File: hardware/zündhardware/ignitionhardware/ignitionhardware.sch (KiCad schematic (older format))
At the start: 25 parts

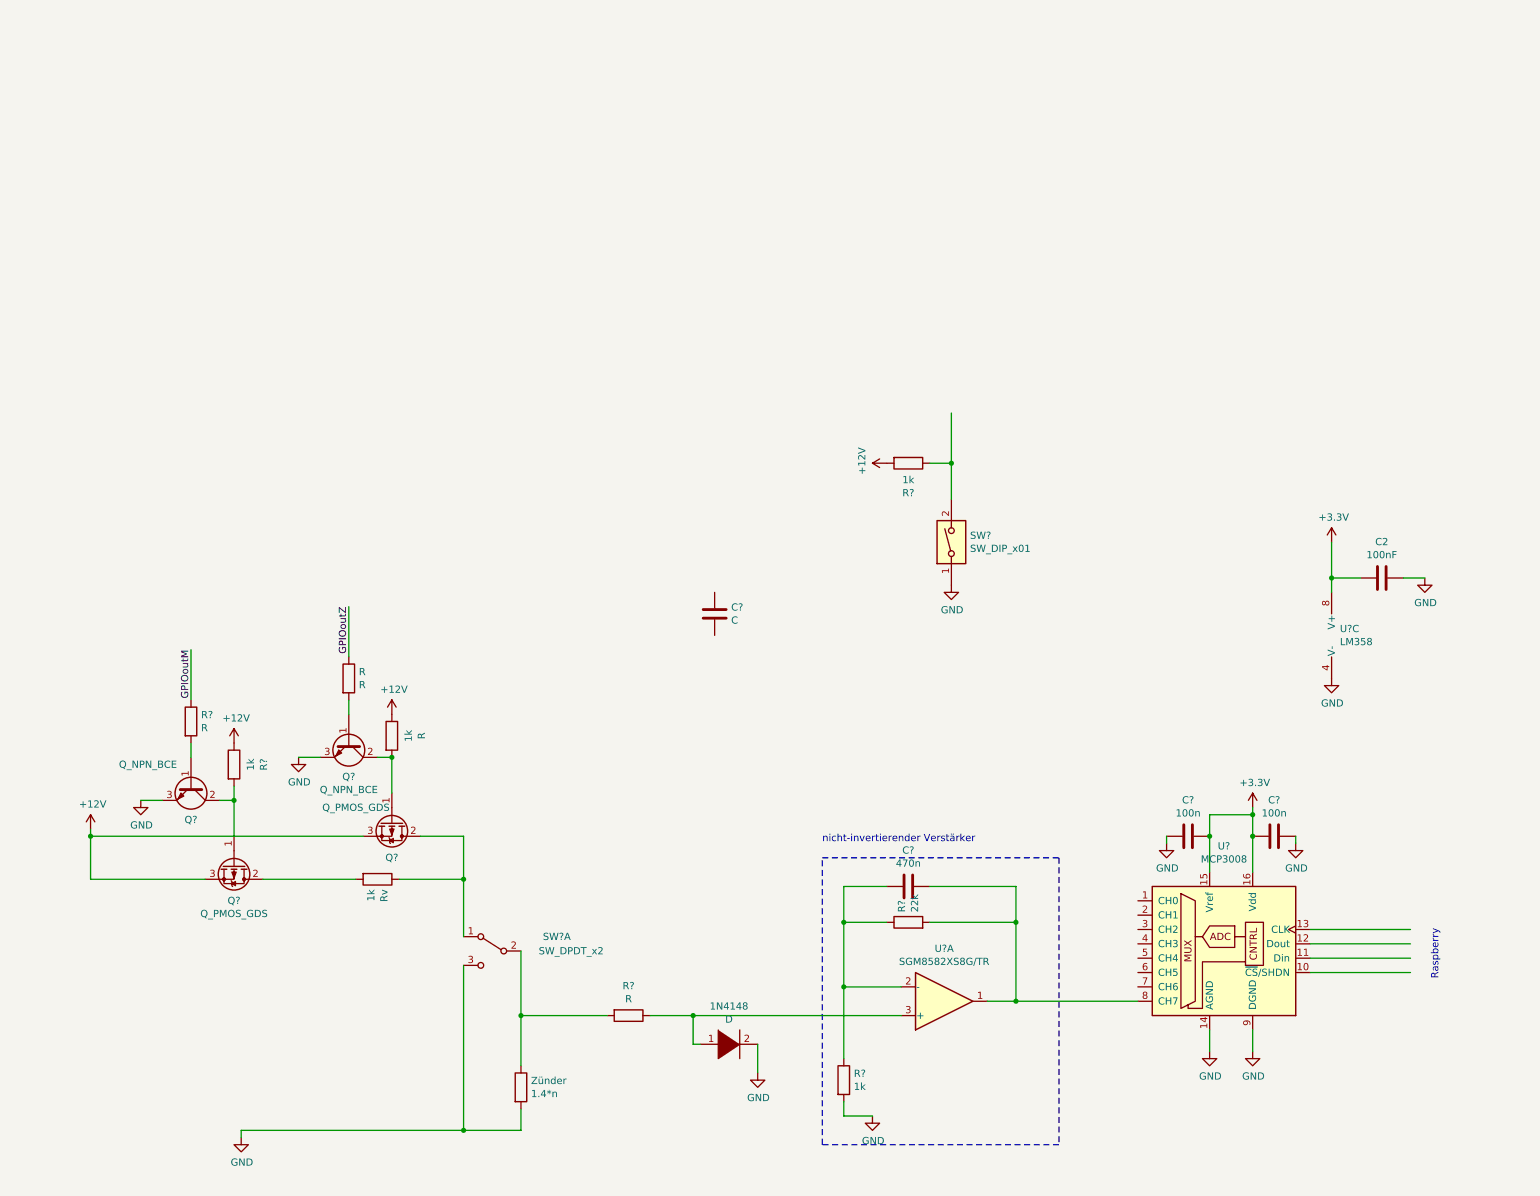
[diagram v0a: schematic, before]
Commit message: updated ignition hardware and created asciidoc description
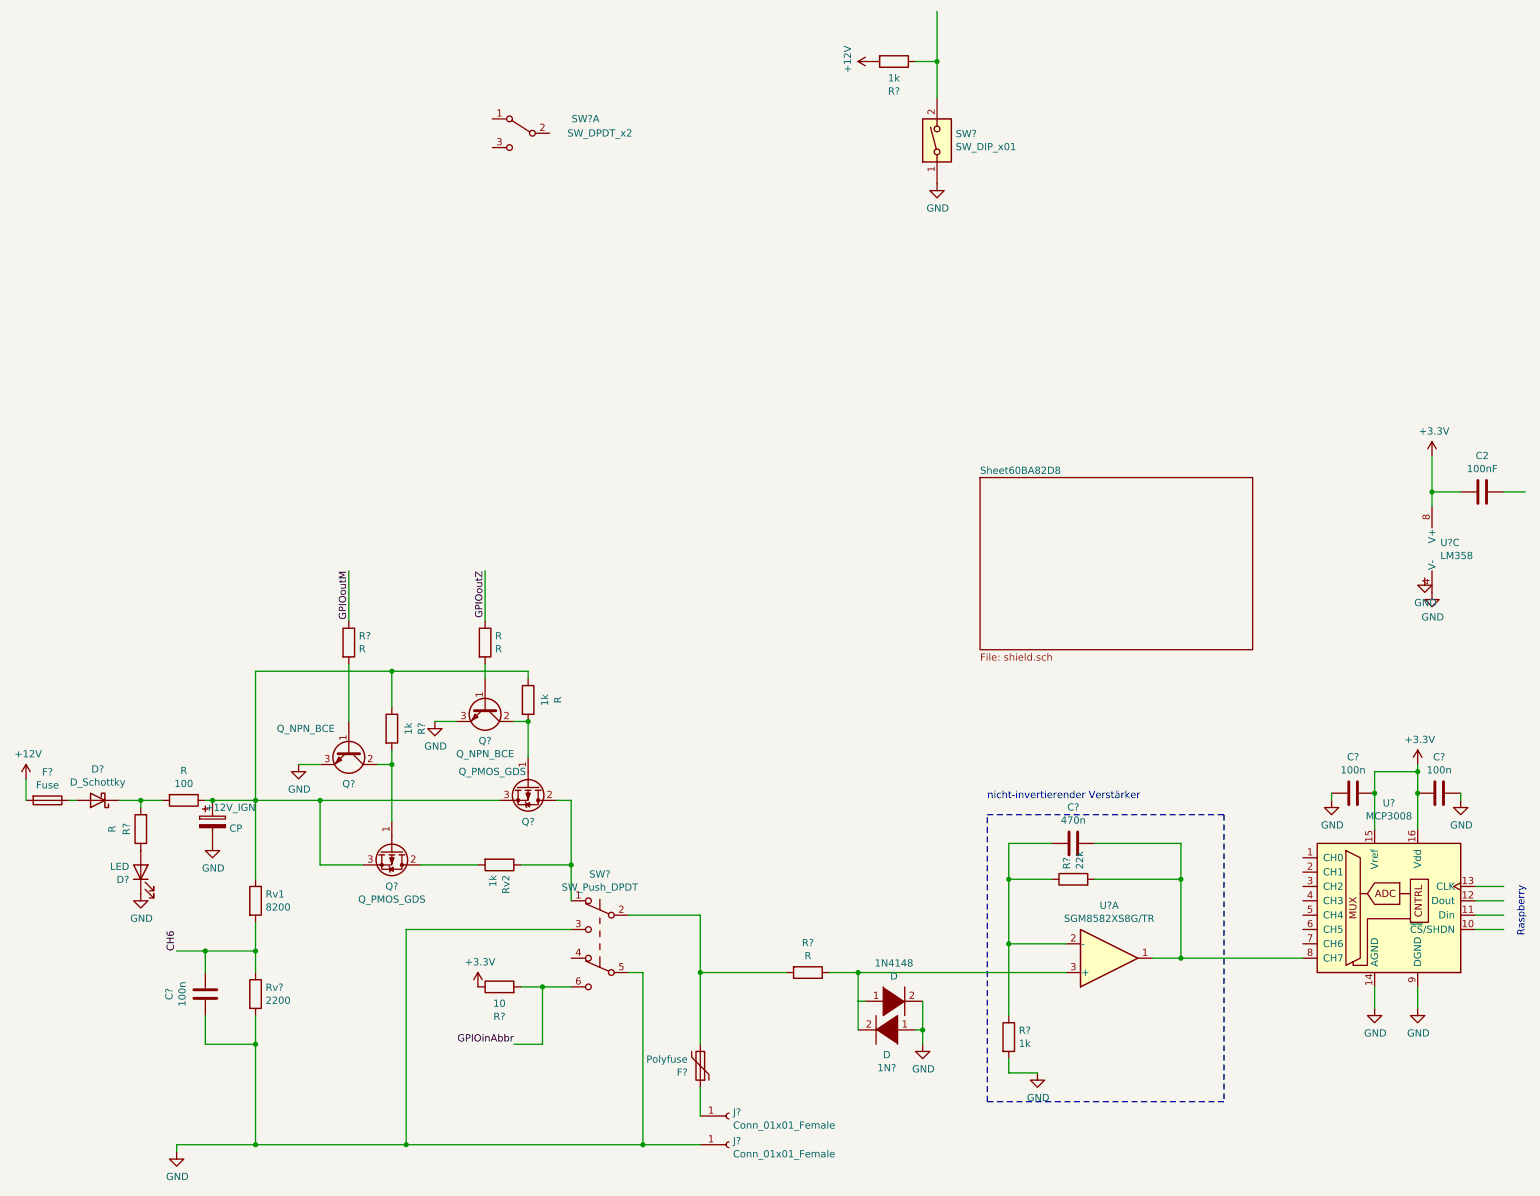
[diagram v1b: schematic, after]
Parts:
- removed C?: C, symbol Device:C
- removed Zünder: 1.4*n, symbol Device:R
- added +12V_IGN: CP, symbol Device:CP
- added 1N?: D, symbol pspice:DIODE
- added C?: 100n, symbol Device:C
- added D?: D_Schottky, symbol Device:D_Schottky
- added D?: LED, symbol Device:LED
- added F?: Polyfuse, symbol Device:Polyfuse
- added F?: Fuse, symbol Device:Fuse
- added J? (x2): Conn_01x01_Female, symbol Connector:Conn_01x01_Female
- added R: 100, symbol Device:R
- added R?: 10, symbol Device:R
- added R?: R, symbol Device:R
- added Rv1: 8200, symbol Device:R
- added Rv?: 2200, symbol Device:R
- added SW?: SW_Push_DPDT, symbol Switch:SW_Push_DPDT
- renumbered Rv to Rv2
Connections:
- net labels added: CH6, GPIOinAbbr
- wire segments 68 -> 103
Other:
- moved on the sheet: 1N4148, C2, C?, Q?, R, R?, Rv2, SW?, SW?A, U?, U?A, U?C
